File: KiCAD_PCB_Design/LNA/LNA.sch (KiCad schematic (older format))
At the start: 12 parts, among them P1 SMA, P2 3V_SUPPLY, P3 SMA, U1 MGA-62563

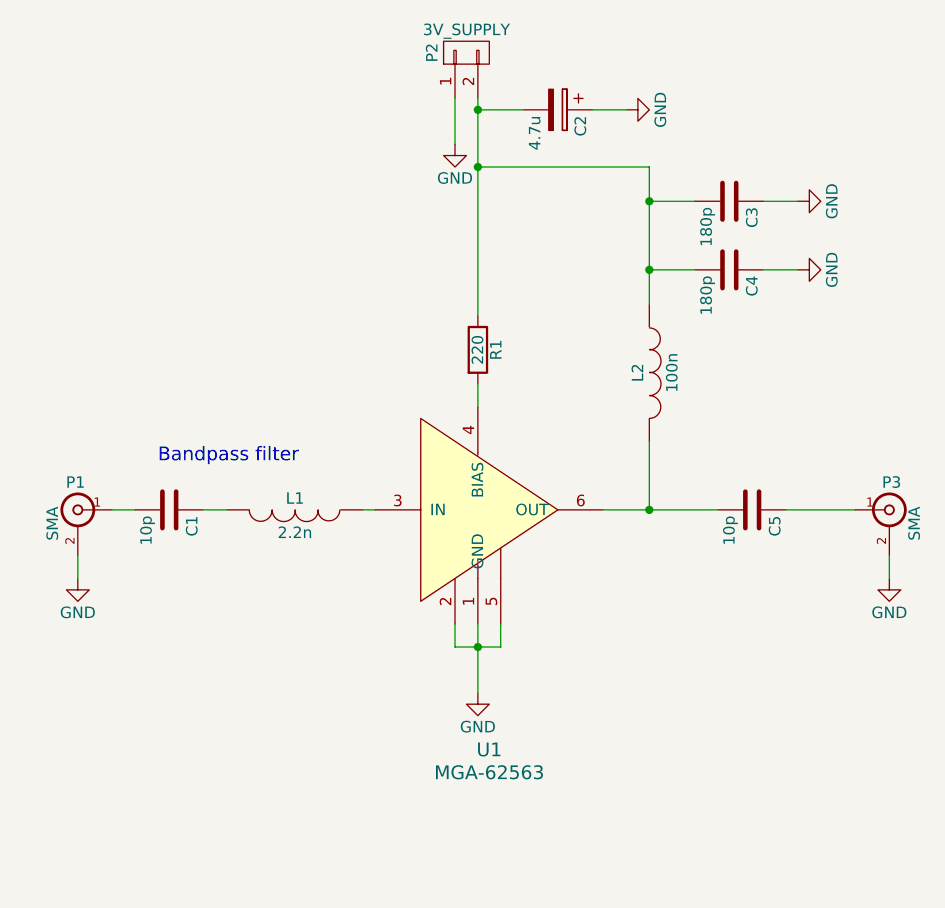
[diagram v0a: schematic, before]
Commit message: All components made except antenna, Now verifying ..
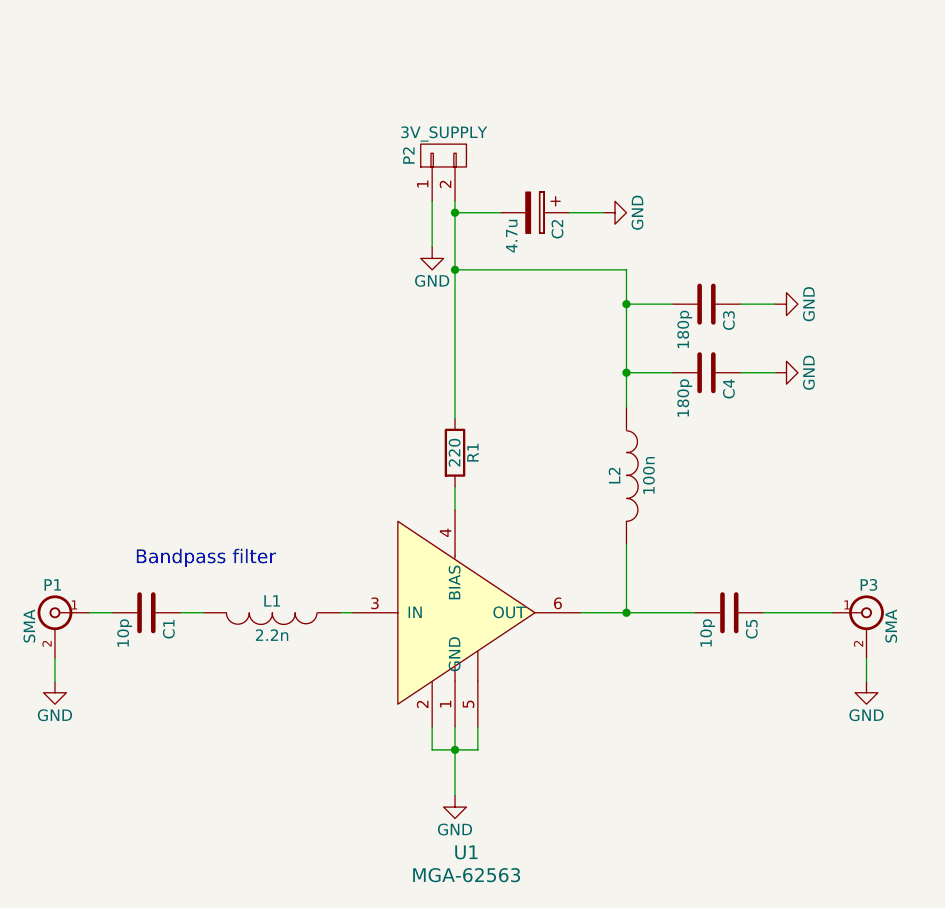
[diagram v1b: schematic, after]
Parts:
- C1, C3, C4, C5: footprint Capacitors_SMD:C_0805 -> Capacitors_SMD:C_0805_HandSoldering
- L1, L2: footprint Custom_Footprints:Inductor_0805 -> Resistors_SMD:R_0805_HandSoldering
- R1: footprint Resistors_SMD:R_0805 -> Resistors_SMD:R_0805_HandSoldering
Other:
- moved on the sheet: C1, C2, C3, C4, C5, L1, L2, P1, P2, P3, R1, U1
